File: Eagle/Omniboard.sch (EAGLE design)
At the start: 58 parts, among them IC1 AP2112K-3.3TRG1 3.3V, Q1 12MHz 3.2x2.5, Q2 BC817, Q3 BC817, Q4 MMBT2222A, SW1 ED_DPDT, U1 CH340T, U2 LMC7101AIM5, U3 MCP73213, U4 DRV8837, U5 DRV8837, U6 DRV8837, X1 ESP-12

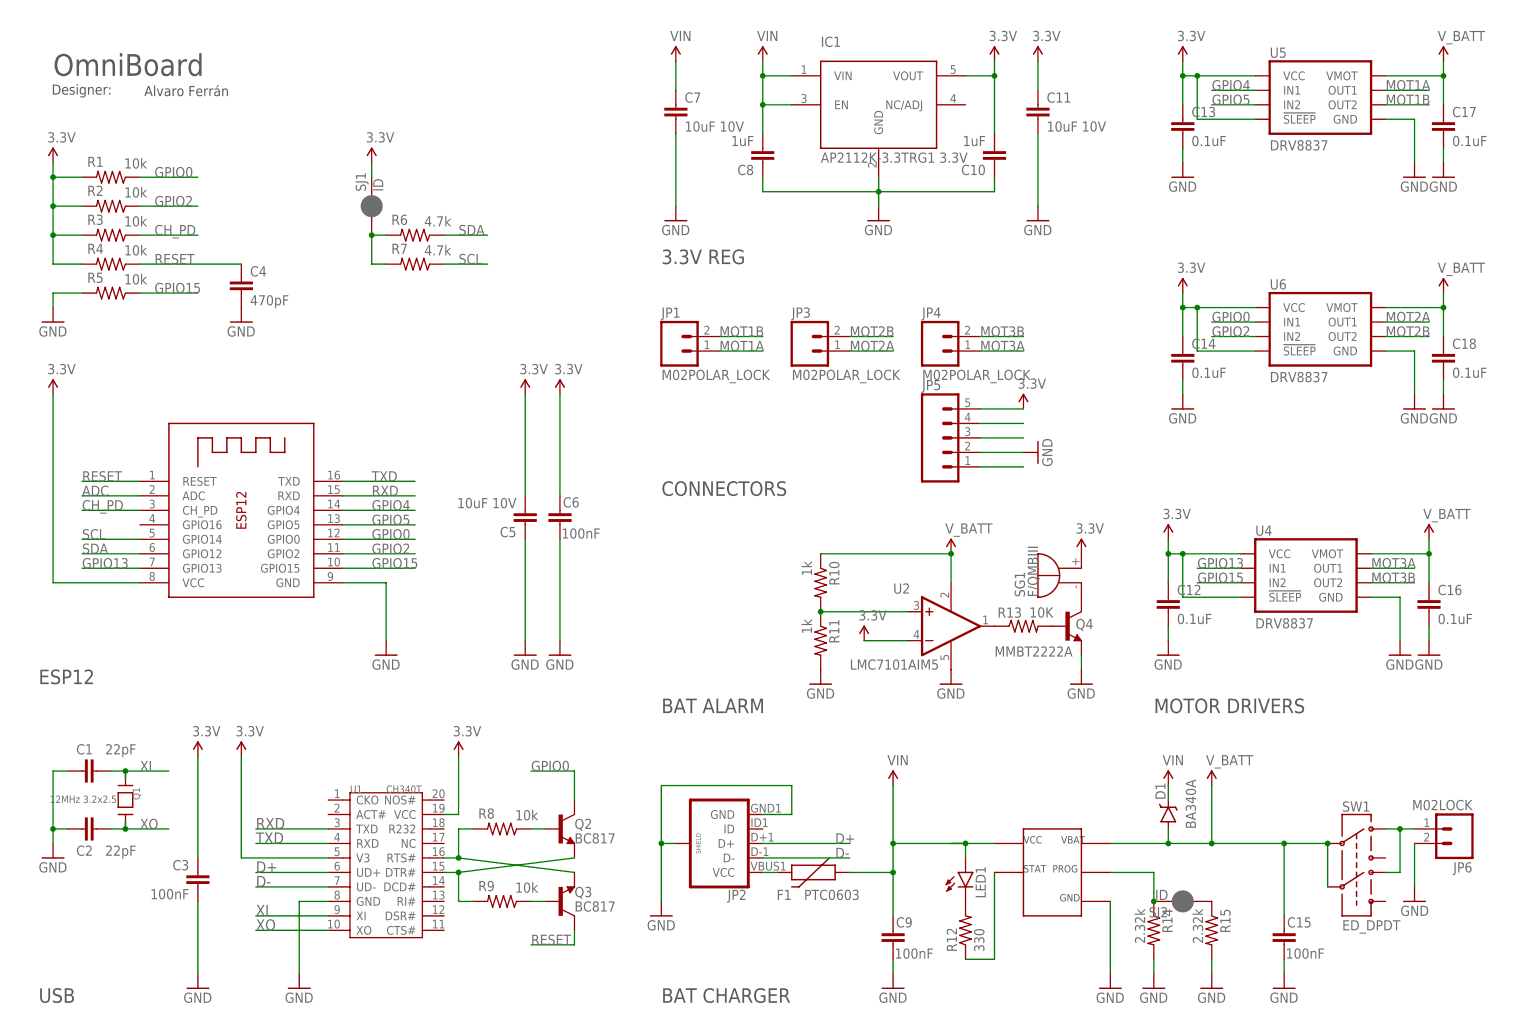
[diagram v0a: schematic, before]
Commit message: Changed to 1S lipo, button added, bugs fixed
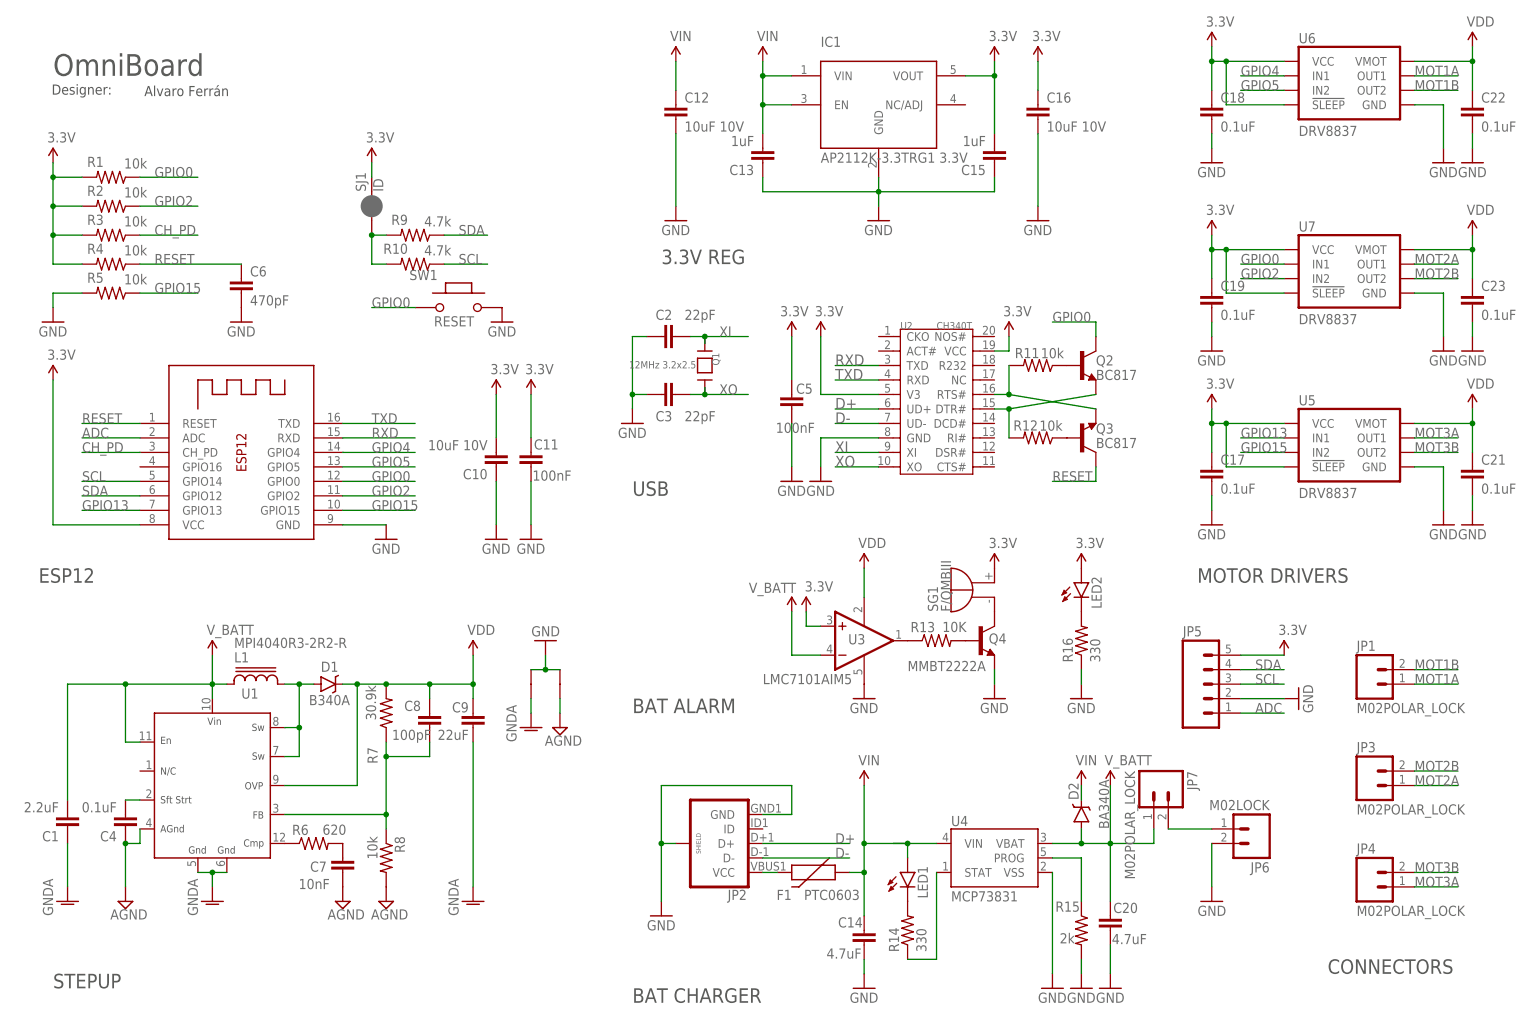
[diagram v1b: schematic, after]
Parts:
- removed SJ2: ID, SparkFun-Passives:JUMPER-PAD-2-NC_BY_PASTE
- added C19, C21, C22, C23: 0.1uF, SparkFun-Capacitors:0.1UF-16V(+-10%)(0402)
- added C20: 4.7uF, SparkFun-Passives:CAP0402-CAP
- added D2: BA340A, SparkFun-DiscreteSemi:B340A
- added GND12, GND16: VIRTUAL_GND, alvaroferran:VIRTUAL_GND
- added JP7: M02POLAR_LOCK, SparkFun-Connectors:M02POLAR_LOCK
- added L1: MPI4040R3-2R2-R, inductor-Eaton Bussmann:MPI4040R3-2R2-R
- added LED2: (no value), SparkFun-LED:LED0603
- added R16: 330, SparkFun-Passives:RESISTOR0402-RES
- added U7: DRV8837, packages(ti):DRV8837
- C1: value 22pF -> 2.2uF; device SparkFun-Passives:CAP0402-CAP -> SparkFun-Passives:CAP0603-CAP
- C10: value 1uF -> 10uF 10V; device SparkFun-Passives:CAP0603-CAP -> SparkFun-Passives:CAP0402-CAP
- C11: value 10uF 10V -> 100nF; device SparkFun-Passives:CAP0603-CAP -> SparkFun-Passives:CAP0402-CAP
- C12, C16: value 0.1uF -> 10uF 10V; device SparkFun-Capacitors:0.1UF-16V(+-10%)(0402) -> SparkFun-Passives:CAP0603-CAP
- C13: value 0.1uF -> 1uF; device SparkFun-Capacitors:0.1UF-16V(+-10%)(0402) -> SparkFun-Passives:CAP0603-CAP
- C14: value 0.1uF -> 4.7uF; device SparkFun-Capacitors:0.1UF-16V(+-10%)(0402) -> SparkFun-Passives:CAP0402-CAP
- C15: value 100nF -> 1uF; device SparkFun-Passives:CAP0402-CAP -> SparkFun-Passives:CAP0603-CAP
- C3: value 100nF -> 22pF
- C4: value 470pF -> 0.1uF; device SparkFun-Passives:CAP0402-CAP -> SparkFun-Passives:CAP0603-CAP
- C5: value 10uF 10V -> 100nF
- C6: value 100nF -> 470pF
- C7: value 10uF 10V -> 10nF
- C8: value 1uF -> 100pF
- C9: value 100nF -> 22uF; device SparkFun-Passives:CAP0402-CAP -> SparkFun-Capacitors:22UF-6.3V-20%(0805)
- D1: value BA340A -> B340A; device SparkFun-DiscreteSemi:B340A -> SparkFun-DiscreteSemi:DIODE-SCHOTTKY-B340A
- R10: value 1k -> 4.7k; device SparkFun-Passives:RESISTOR0402-RES -> resistor:R-US_R0402
- R11: value 1k -> 10k; device SparkFun-Passives:RESISTOR0402-RES -> resistor:R-US_R0402
- R12: value 330 -> 10k; device SparkFun-Passives:RESISTOR0402-RES -> resistor:R-US_R0402
- R14: value 2.32k -> 330
- R15: value 2.32k -> 2k
- R6: value 4.7k -> 620; device resistor:R-US_R0402 -> SparkFun-Passives:RESISTOR0603-RES
- R7: value 4.7k -> 30.9k; device resistor:R-US_R0402 -> SparkFun-Passives:RESISTOR0603-RES
- R8: device resistor:R-US_R0402 -> SparkFun-Passives:RESISTOR0603-RES
- R9: value 10k -> 4.7k
- SW1: value ED_DPDT -> RESET; device pighiXXX:ED_DPDT -> MySMD:PB157
- U1: value CH340T -> (none); device template:CH340T -> MIC2253_MLF12:MIC2253
- U2: value LMC7101AIM5 -> CH340T; device linear:LMC7101AIM5 -> template:CH340T
- U3: value MCP73213 -> LMC7101AIM5; device alvaroferran:MCP73213 -> linear:LMC7101AIM5
- U4: value DRV8837 -> MCP73831; device packages(ti):DRV8837 -> SparkFun-PowerIC:MCP73831
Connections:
- new net AGND: C4.1, C7.1, GND16.P$1, R8.2, U1.AGND
- new net N$16: R6.1, U1.CMP
- new net N$24: C8.1, R7.1, R8.1, U1.FB
- new net N$3: C7.2, R6.2
- new net N$4: C4.2, U1.SS
- new net PGND: C1.1, C9.1, GND12.P$1, U1.GND@1, U1.GND@2
- new net VDD: C21.1, C22.1, C23.1, C8.2, C9.2, D1.C, R7.2, U1.OVP, U3.V+, U5.VMOT, U6.VMOT, U7.VMOT
- net 3.3V: now also C15.2, C16.1, C17.1, C18.1, C19.1, LED2.A, U2.V3, U2.VCC, U3.+IN, U7.!SLEEP, U7.VCC; no longer C12.1, C13.1, C14.1, C3.2, C6.1, U1.V3, U1.VCC, U2.-IN, U4.!SLEEP, U4.VCC
- net D+: now also U2.UD+; no longer U1.UD+
- net D-: now also U2.UD-; no longer U1.UD-
- net GND: now also C13.1, C15.1, C19.2, C20.2, C21.2, C22.2, C23.2, GND12.P$2, GND16.P$2, R16.1, SW1.2, U2.GND, U3.V-, U4.VSS, U7.GND; no longer C1.1, C13.2, C15.2, C4.2, C7.2, C8.1, C9.2, R11.2, R14.2, U1.GND, U2.V-, U3.GND, U4.GND
- net GPIO0: now also SW1.1, U7.IN1; no longer U6.IN1
- net GPIO13: now also U5.IN1; no longer U4.IN1
- net GPIO15: now also U5.IN2; no longer U4.IN2
- net GPIO2: now also U7.IN2; no longer U6.IN2
- net GPIO4: now also U6.IN1; no longer U5.IN1
- net GPIO5: now also U6.IN2; no longer U5.IN2
- net MOT1A: now also U6.OUT1; no longer U5.OUT1
- net MOT1B: now also U6.OUT2; no longer U5.OUT2
- net MOT2A: now also U7.OUT1; no longer U6.OUT1
- net MOT2B: now also U7.OUT2; no longer U6.OUT2
- net MOT3A: now also U5.OUT1; no longer U4.OUT1
- net MOT3B: now also U5.OUT2; no longer U4.OUT2
- net N$1: now also R10.2, R9.2; no longer R6.2, R7.2
- net N$10: now also R11.2, U2.RTS#; no longer R8.2, U1.RTS#
- net N$11: now also R15.1, U4.PROG; no longer R14.1, SJ2.2, U3.PROG
- net N$12: now also D1.A, L1.2, U1.SW@1, U1.SW@2; no longer R15.1, SJ2.1
- net N$13: now also R14.1, U4.STAT; no longer R12.1, U3.STAT
- net N$15: now also LED2.C, R16.2; no longer R10.2, R11.1, U2.+IN
- net N$17: now also U3.OUT; no longer U2.OUT
- net N$2: now also R12.2, U2.DTR#; no longer R9.2, U1.DTR#
- net N$5: now also R14.2; no longer R12.2
- net N$6: now also R11.1; no longer R8.1
- net N$7: now also R12.1; no longer R9.1
- net RESET: now also C6.1; no longer C4.1
- net RXD: now also U2.TXD; no longer U1.TXD
- net SCL: now also R10.1; no longer R7.1
- net SDA: now also R9.1; no longer R6.1
- net TXD: now also U2.RXD; no longer U1.RXD
- net VBAT: now also JP7.2; no longer SW1.1, SW1.4
- net VIN: now also C12.1, C13.2, C14.1, D2.C, U4.VIN; no longer C7.1, C8.2, C9.1, D1.C, U3.VCC
- net V_BATT: now also C1.2, C20.1, D2.A, JP7.1, L1.1, U1.EN, U1.VIN, U3.-IN, U4.VBAT; no longer C15.1, C16.1, C17.1, C18.1, D1.A, R10.1, SW1.2, SW1.5, U2.V+, U3.VBAT, U4.VMOT, U5.VMOT, U6.VMOT
- net XI: now also C2.2, U2.XI; no longer C1.2, U1.XI
- net XO: now also C3.2, U2.XO; no longer C2.2, U1.XO
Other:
- note added: "STEPUP"
- moved on the sheet: C1, C10, C11, C12, C13, C14, C15, C16, C17, C18, C2, C3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

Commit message: Project updated
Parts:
- C10: value 10uF 10V -> 22pF
- C11: value 100nF -> 22pF
- C12: value 10uF 10V -> 1uF
- C13: value 1uF -> 100nF; device SparkFun-Passives:CAP0603-CAP -> SparkFun-Passives:CAP0402-CAP
- C17: value 0.1uF -> 4.7uF; device SparkFun-Capacitors:0.1UF-16V(+-10%)(0402) -> SparkFun-Passives:CAP0402-CAP
- C2: value 22pF -> 0.1uF; device SparkFun-Passives:CAP0402-CAP -> SparkFun-Passives:CAP0603-CAP
- C20: value 4.7uF -> 0.1uF; device SparkFun-Passives:CAP0402-CAP -> SparkFun-Capacitors:0.1UF-16V(+-10%)(0402)
- C3: value 22pF -> 470pF
- C4: value 0.1uF -> 10nF
- C5: value 100nF -> 100pF; device SparkFun-Passives:CAP0402-CAP -> SparkFun-Passives:CAP0603-CAP
- C6: value 470pF -> 22uF; device SparkFun-Passives:CAP0402-CAP -> SparkFun-Capacitors:22UF-6.3V-20%(0805)
- C7: value 10nF -> 10uF 10V; device SparkFun-Passives:CAP0603-CAP -> SparkFun-Passives:CAP0402-CAP
- C8: value 100pF -> 100nF; device SparkFun-Passives:CAP0603-CAP -> SparkFun-Passives:CAP0402-CAP
- C9: value 22uF -> 10uF 10V; device SparkFun-Capacitors:22UF-6.3V-20%(0805) -> SparkFun-Passives:CAP0603-CAP
- JP1: value M02POLAR_LOCK -> USB_MICROB; device SparkFun-Connectors:M02POLAR_LOCK -> SparkFun-Connectors:USB_MICROB_PLUGCONN-11752
- JP2: value USB_MICROB_PLUGCONN-11752 -> M02POLAR_LOCK; device SparkFun-Connectors:USB_MICROB_PLUGCONN-11752 -> SparkFun-Connectors:M02POLAR_LOCK
- JP3: value M02POLAR_LOCK -> (none); device SparkFun-Connectors:M02POLAR_LOCK -> SparkFun-Connectors:M05LOCK
- JP4: value M02POLAR_LOCK -> M02LOCK; device SparkFun-Connectors:M02POLAR_LOCK -> SparkFun-Connectors:M02LOCK
- JP5: value (none) -> M02POLAR_LOCK; device SparkFun-Connectors:M05LOCK -> SparkFun-Connectors:M02POLAR_LOCK
- JP6: value M02LOCK -> M02POLAR_LOCK; device SparkFun-Connectors:M02LOCK -> SparkFun-Connectors:M02POLAR_LOCK
- Q2: value BC817 -> MMBT2222A; device transistor-npn:BC817-16SMD -> SparkFun-DiscreteSemi:TRANSISTOR_NPNMMBT2222A
- Q4: value MMBT2222A -> BC817; device SparkFun-DiscreteSemi:TRANSISTOR_NPNMMBT2222A -> transistor-npn:BC817-16SMD
- R11: value 10k -> 330; device resistor:R-US_R0402 -> SparkFun-Passives:RESISTOR0402-RES
- R12: value 10k -> 10K; device resistor:R-US_R0402 -> SparkFun:RESISTOR0402-RES
- R13: value 10K -> 10k; device SparkFun:RESISTOR0402-RES -> resistor:R-US_R0402
- R14: value 330 -> 10k; device SparkFun-Passives:RESISTOR0402-RES -> resistor:R-US_R0402
- R15: value 2k -> 330
- R16: value 330 -> 2k
- U2: value CH340T -> LMC7101AIM5; device template:CH340T -> linear:LMC7101AIM5
- U3: value LMC7101AIM5 -> CH340T; device linear:LMC7101AIM5 -> template:CH340T
- renumbered GND12 to GND10, GND16 to GND13
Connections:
- net 3.3V: now also C13.2, C20.1, C7.2, C8.1, JP3.5, U2.+IN, U3.V3, U3.VCC; no longer C10.2, C11.1, C17.1, C5.2, JP5.5, U2.V3, U2.VCC, U3.+IN
- net ADC: now also JP3.1; no longer JP5.1
- net AGND: now also C2.1; no longer C7.1
- net D+: now also JP1.D+, U3.UD+; no longer JP2.D+, U2.UD+
- net D-: now also JP1.D-, U3.UD-; no longer JP2.D-, U2.UD-
- net GND: now also C11.1, C12.1, C3.2, C7.1, C8.2, C9.2, JP1.GND, JP1.SHIELD, JP3.2, JP4.2, Q2.E, R15.1, R16.2, U2.V-, U3.GND; no longer C11.2, C12.2, C2.1, C3.1, C5.1, C6.2, JP2.GND, JP2.SHIELD, JP5.2, JP6.2, Q4.E, R15.2, R16.1, U2.GND, U3.V-
- net GPIO0: now also Q3.C, U6.IN1; no longer Q2.C, U7.IN1
- net GPIO13: now also U7.IN1; no longer U5.IN1
- net GPIO15: now also U7.IN2; no longer U5.IN2
- net GPIO2: now also U6.IN2; no longer U7.IN2
- net GPIO4: now also U5.IN1; no longer U6.IN1
- net GPIO5: now also U5.IN2; no longer U6.IN2
- net MOT1A: now also JP5.1, U5.OUT1; no longer JP1.1, U6.OUT1
- net MOT1B: now also JP5.2, U5.OUT2; no longer JP1.2, U6.OUT2
- net MOT2A: now also JP6.1, U6.OUT1; no longer JP3.1, U7.OUT1
- net MOT2B: now also JP6.2, U6.OUT2; no longer JP3.2, U7.OUT2
- net MOT3A: now also JP7.1, U7.OUT1; no longer JP4.1, U5.OUT1
- net MOT3B: now also JP7.2, U7.OUT2; no longer JP4.2, U5.OUT2
- net N$10: now also Q4.E, R13.2, U3.RTS#; no longer Q3.E, R11.2, U2.RTS#
- net N$11: now also R16.1; no longer R15.1
- net N$13: now also R11.1; no longer R14.1
- net N$14: now also JP1.VCC; no longer JP2.VCC
- net N$15: now also R15.2; no longer R16.2
- net N$17: now also R12.1, U2.OUT; no longer R13.1, U3.OUT
- net N$2: now also Q3.E, R14.2, U3.DTR#; no longer Q2.E, R12.2, U2.DTR#
- net N$24: now also C5.1; no longer C8.1
- net N$3: now also C4.2; no longer C7.2
- net N$4: now also C2.2; no longer C4.2
- net N$5: now also R11.2; no longer R14.2
- net N$6: now also Q3.B, R13.1; no longer Q2.B, R11.1
- net N$7: now also Q4.B, R14.1; no longer Q3.B, R12.1
- net N$8: now also Q2.B, R12.2; no longer Q4.B, R13.2
- net N$9: now also Q2.C; no longer Q4.C
- net PGND: now also C6.1; no longer C9.1
- net RESET: now also C3.1, Q4.C; no longer C6.1, Q3.C
- net RXD: now also U3.TXD; no longer U2.TXD
- net SCL: now also JP3.3; no longer JP5.3
- net SDA: now also JP3.4; no longer JP5.4
- net TXD: now also U3.RXD; no longer U2.RXD
- net VBAT: now also JP2.2, JP4.1; no longer JP6.1, JP7.2
- net VDD: now also C5.2, C6.2, U2.V+; no longer C8.2, C9.2, U3.V+
- net VIN: now also C12.2, C9.1; no longer C12.1, C13.2
- net V_BATT: now also C17.1, JP2.1, U2.-IN; no longer C20.1, JP7.1, U3.-IN
- net XI: now also C10.2, U3.XI; no longer C2.2, U2.XI
- net XO: now also C11.2, U3.XO; no longer C3.2, U2.XO
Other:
- moved on the sheet: C10, C11, C12, C13, C17, C2, C20, C21, C22, C23, C3, C4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
